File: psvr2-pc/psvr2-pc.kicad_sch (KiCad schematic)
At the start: 89 parts, among them IC1 SN65MLVD200D, IC2 SN65MLVD200D, J1 USB_C_Receptacle, J2 USB3_B_Micro, J3 DP_47272, J4 Barrel_Jack_Switch, J5 Conn_01x02_Pin, Q1 Si2301CDS, Q2 PN2222A, Q3 Si2301CDS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

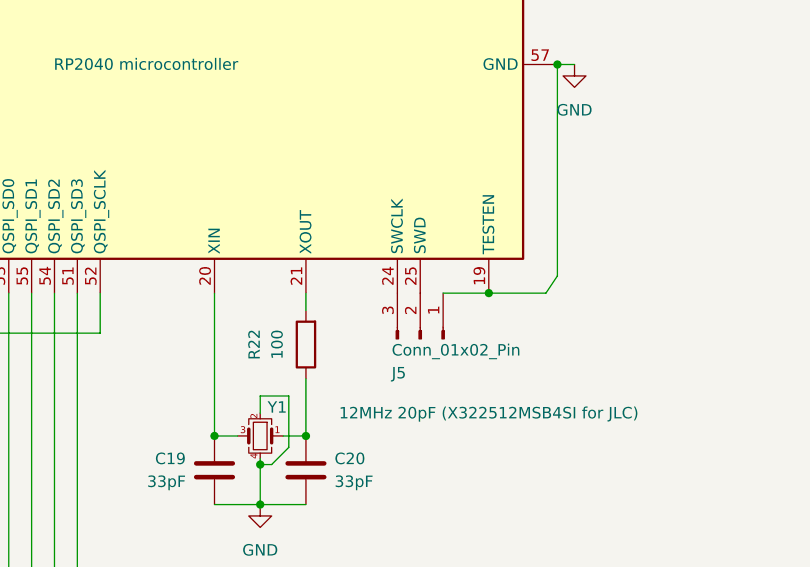
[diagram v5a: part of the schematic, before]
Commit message: Fix the VBUS_5V net not getting renamed into the PCB editor from the schematic due to an error with the diode footprint. Change it and now it works. Add the 5V power traces and keep connecting more stuff, only like 22 DRC problems found now. ¯\_(ツ)_/¯
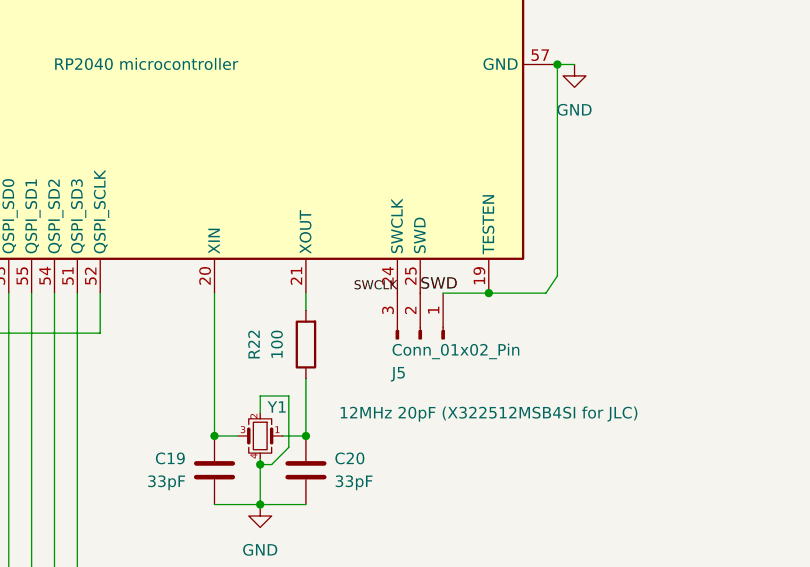
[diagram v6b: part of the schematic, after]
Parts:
- D1: footprint Diode_SMD_AKL:D_SMA -> Diode_SMD:D_0805_2012Metric
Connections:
- net SWD: now reaches J5.2 (Pin_2), U1.25 (SWD)
- net SWCLK: now reaches J5.3 (Pin_3), U1.24 (SWCLK)
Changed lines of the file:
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@@
     (effects (font (size 1.27 1.27)) (justify right bottom))
+  )
+  (label "SWD" (at 208.915 200.025 0) (fields_autoplaced)
+    (effects (font (size 1.27 1.27)) (justify left bottom))
+  )
+  (label "SWCLK" (at 206.375 200.025 180) (fields_autoplaced)
+    (effects (font (size 1 1)) (justify right bottom))
   )
   (label "HMD_LVDS_DE" (at 163.195 149.225 90) (fields_autoplaced)
@@
       (effects (font (size 1.27 1.27)))
     )
-    (property "Footprint" "Diode_SMD_AKL:D_SMA" (at 44.45 85.09 0)
-      (effects (font (size 1.27 1.27)) hide)
-    )
+    (property "Footprint" "Diode_SMD:D_0805_2012Metric" (at 44.45 85.09 0)
+      (effects (font (size 1.27 1.27)) hide)
+    )

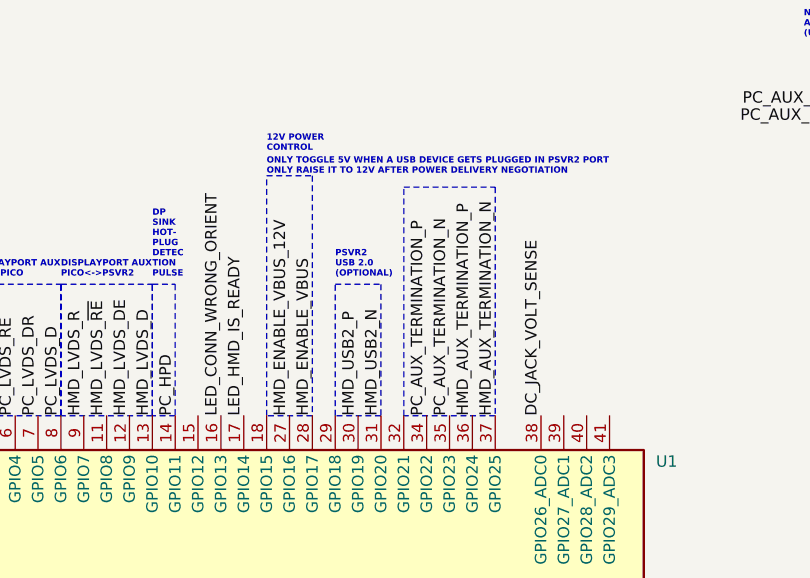
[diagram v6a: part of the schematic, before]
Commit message: Route the DP-AUX pull-up/pull-down GPIOs, had to switch them around for the traces to line up without overlapping. Make it do a nice pattern/shape, surrounding each island. Why not.
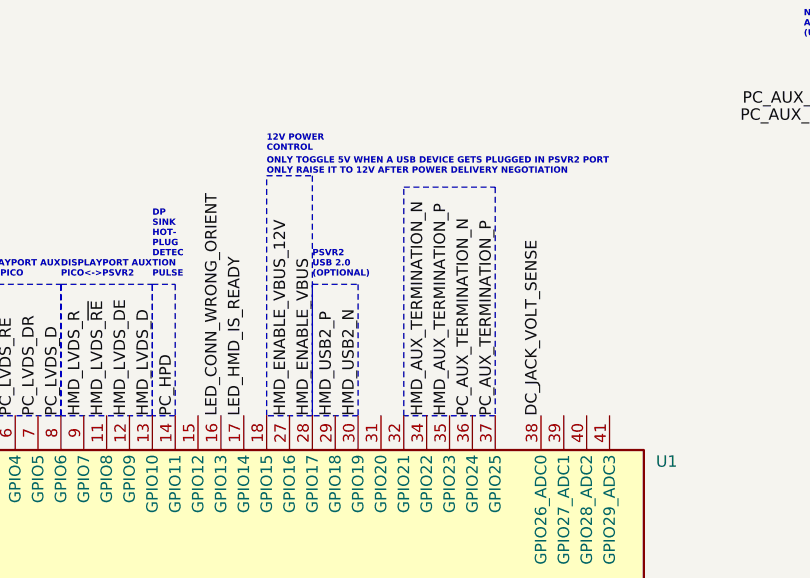
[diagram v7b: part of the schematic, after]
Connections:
- net HMD_AUX_TERMINATION_N: now also U1.34 (GPIO22); no longer U1.37 (GPIO25)
- net HMD_AUX_TERMINATION_P: now also U1.35 (GPIO23); no longer U1.36 (GPIO24)
- net HMD_USB2_N: now also U1.30 (GPIO19); no longer U1.31 (GPIO20)
- net HMD_USB2_P: now also U1.29 (GPIO18); no longer U1.30 (GPIO19)
- net PC_AUX_TERMINATION_N: now also U1.36 (GPIO24); no longer U1.35 (GPIO23)
- net PC_AUX_TERMINATION_P: now also U1.37 (GPIO25); no longer U1.34 (GPIO22)
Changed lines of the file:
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@@
     (fill (type none))
   )
-  (rectangle (start 186.055 134.62) (end 191.135 149.225)
+  (rectangle (start 183.515 134.62) (end 188.595 149.225)
     (stroke (width 0) (type dot))
     (fill (type none))
@@
     (effects (font (size 0.7 0.7) bold) (justify left bottom))
   )
-  (text "PSVR2\nUSB 2.0\n(OPTIONAL)" (at 186.055 133.985 0)
+  (text "PSVR2\nUSB 2.0\n(OPTIONAL)" (at 183.515 133.985 0)
     (effects (font (size 0.7 0.7) bold) (justify left bottom))
   )
@@
     (effects (font (size 1.27 1.27)) (justify left bottom))
   )
+  (label "HMD_AUX_TERMINATION_P" (at 198.755 149.225 90) (fields_autoplaced)
+    (effects (font (size 1.27 1.27)) (justify left bottom))
+  )
   (label "HMD_AUX_P" (at 250.19 95.25 180) (fields_autoplaced)
     (effects (font (size 1.27 1.27)) (justify right bottom))
@@
     (effects (font (size 1.27 1.27)) (justify left bottom))
   )
+  (label "PC_AUX_TERMINATION_N" (at 201.295 149.225 90) (fields_autoplaced)
+    (effects (font (size 1.27 1.27)) (justify left bottom))
+  )
   (label "PC_AUX_P" (at 306.07 146.05 0) (fields_autoplaced)
     (effects (font (size 1.27 1.27)) (justify left bottom))
@@
     (effects (font (size 1.27 1.27)) (justify left bottom))
   )
-  (label "PC_AUX_TERMINATION_P" (at 196.215 149.225 90) (fields_autoplaced)
-    (effects (font (size 1.27 1.27)) (justify left bottom))
-  )
-  (label "HMD_USB2_N" (at 191.135 149.225 90) (fields_autoplaced)
-    (effects (font (size 1.27 1.27)) (justify left bottom))
-  )
   (label "PC_AUX_N" (at 306.07 161.29 0) (fields_autoplaced)
     (effects (font (size 1.27 1.27)) (justify left bottom))
@@
     (effects (font (size 1.27 1.27)) (justify left bottom))
   )
-  (label "HMD_AUX_TERMINATION_P" (at 201.295 149.225 90) (fields_autoplaced)
-    (effects (font (size 1.27 1.27)) (justify left bottom))
-  )
   (label "LED_HMD_IS_READY" (at 377.19 33.655 0) (fields_autoplaced)
     (effects (font (size 1.27 1.27)) (justify left bottom))
@@
     (effects (font (size 1.27 1.27)) (justify left bottom))
   )
-  (label "HMD_USB2_P" (at 188.595 149.225 90) (fields_autoplaced)
+  (label "HMD_USB2_P" (at 186.055 149.225 90) (fields_autoplaced)
     (effects (font (size 1.27 1.27)) (justify left bottom))
   )
@@
     (effects (font (size 1.27 1.27)) (justify left bottom))
   )
+  (label "HMD_AUX_TERMINATION_N" (at 196.215 149.225 90) (fields_autoplaced)
+    (effects (font (size 1.27 1.27)) (justify left bottom))
+  )
   (label "HMD_LVDS_~{RE}" (at 160.655 149.225 90) (fields_autoplaced)
     (effects (font (size 1.27 1.27)) (justify left bottom))
@@
     (effects (font (size 1.27 1.27)) (justify left bottom))
   )
-  (label "HMD_AUX_TERMINATION_N" (at 203.835 149.225 90) (fields_autoplaced)
-    (effects (font (size 1.27 1.27)) (justify left bottom))
-  )
   (label "LED_HMD_IS_READY" (at 175.895 149.225 90) (fields_autoplaced)
     (effects (font (size 1.27 1.27)) (justify left bottom))
@@
   )
   (label "HMD_TYC_SCL" (at 142.875 149.225 90) (fields_autoplaced)
+    (effects (font (size 1.27 1.27)) (justify left bottom))
+  )
+  (label "HMD_USB2_N" (at 188.595 149.225 90) (fields_autoplaced)
     (effects (font (size 1.27 1.27)) (justify left bottom))
   )
@@
     (effects (font (size 1.27 1.27)) (justify right bottom))
   )
-  (label "PC_AUX_TERMINATION_N" (at 198.755 149.225 90) (fields_autoplaced)
-    (effects (font (size 1.27 1.27)) (justify left bottom))
-  )
+  (label "PC_AUX_TERMINATION_P" (at 203.835 149.225 90) (fields_autoplaced)
+    (effects (font (size 1.27 1.27)) (justify left bottom))
+  )

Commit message: Start adding the JLC part codes so that the bill of materials already has that column included and parts get chosen automatically thanks to this handy plugin:
https://github.com/bennymeg/JLC-Plugin-for-KiCad
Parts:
- U1: LCSC Part # (none) -> C2040; Mfr. Part # (none) -> RP2040
- U2: LCSC Part # (none) -> C97521; Mfr. Part # (none) -> W25Q128JVSIQ
- U3: LCSC Part # (none) -> C442699; Mfr. Part # (none) -> Fusb302mpx
- Y1: LCSC Part # (none) -> C9002; Mfr. Part # (none) -> X322512MSB4SI
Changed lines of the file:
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@@
+      (effects (font (size 1.27 1.27)) hide)
+    )
+    (property "Mfr. Part #" "Fusb302mpx" (at 227.965 44.45 0)
+      (effects (font (size 1.27 1.27)) hide)
+    )
+    (property "LCSC Part #" "C442699" (at 227.965 44.45 0)
       (effects (font (size 1.27 1.27)) hide)
     )
@@
       (effects (font (size 1.27 1.27)) hide)
     )
+    (property "LCSC Part #" "C9002" (at 191.135 215.9 0)
+      (effects (font (size 1.27 1.27)) hide)
+    )
+    (property "Mfr. Part #" "X322512MSB4SI" (at 191.135 215.9 0)
+      (effects (font (size 1.27 1.27)) hide)
+    )
     (pin "1")
     (pin "2")
@@
     )
     (property "Datasheet" "http://www.winbond.com/resource-files/w25q128jv_dtr%20revc%2003272018%20plus.pdf" (at 165.735 248.92 0)
+      (effects (font (size 1.27 1.27)) hide)
+    )
+    (property "LCSC Part #" "C97521" (at 165.735 248.92 0)
+      (effects (font (size 1.27 1.27)) hide)
+    )
+    (property "Mfr. Part #" "W25Q128JVSIQ" (at 165.735 248.92 0)
       (effects (font (size 1.27 1.27)) hide)
     )
@@
       (effects (font (size 1.27 1.27)) hide)
     )
+    (property "LCSC Part #" "C2040" (at 178.435 174.625 90)
+      (effects (font (size 1.27 1.27)) hide)
+    )
+    (property "Mfr. Part #" "RP2040" (at 178.435 174.625 90)
+      (effects (font (size 1.27 1.27)) hide)
+    )
